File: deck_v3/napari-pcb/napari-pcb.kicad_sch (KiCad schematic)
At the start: 62 parts, among them J1 USB_C_Receptacle_USB2.0_16P, J11 DNP, J12 CONN_PB_SIG, J13 CONN_PB_GND, J14 CONN_PB_VDD, J17 CONN_PD_SIG, J18 CONN_GND, J19 CONN_VDD, J2 Cirque, J20 CONN_PD_GND, J21 CONN_PD_VDD, J3 Cirque, J4 CONN_ENC_DEV, J5 Cirque A MCU, J6 CONN_ENC_MCU, J7 Cirque B MCU, J8 CONN_PA_SIG, J9 CONN_PA_GND, SW1 SW_Push, SW10 SW_Push, SW11 SW_Push, SW12 SW_Push, SW13 SW_Push, SW14 SW_Push, SW15 SW_Push, SW16 SW_Push, SW2 SW_Push, SW3 SW_Push, SW4 SW_Push, SW5 SW_Push, SW6 SW_Push, SW7 SW_Push, SW8 SW_Push, SW9 SW_Push, U1 STM32G0B1RETx, U2 LD1117S33TR_SOT223

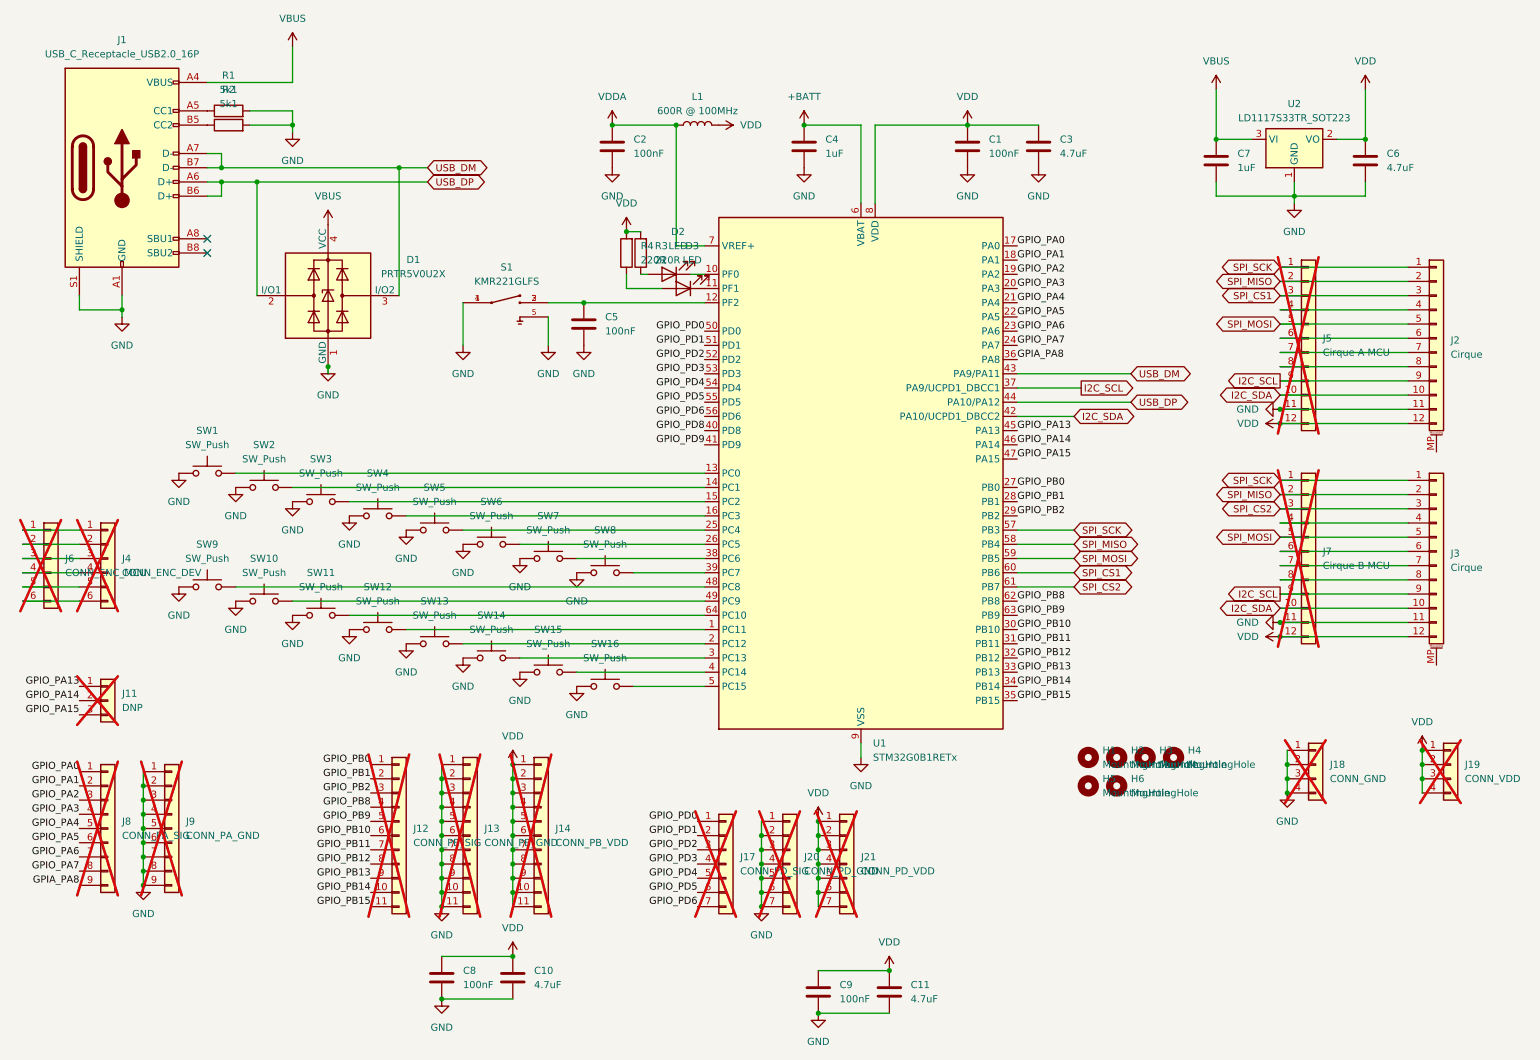
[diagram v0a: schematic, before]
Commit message: deck_v3: Tweak schematic layout for improved visibility of components.
No electrical change.

Signed-off-by: Damien George <dpgeorge@georgerobotics.com.au>
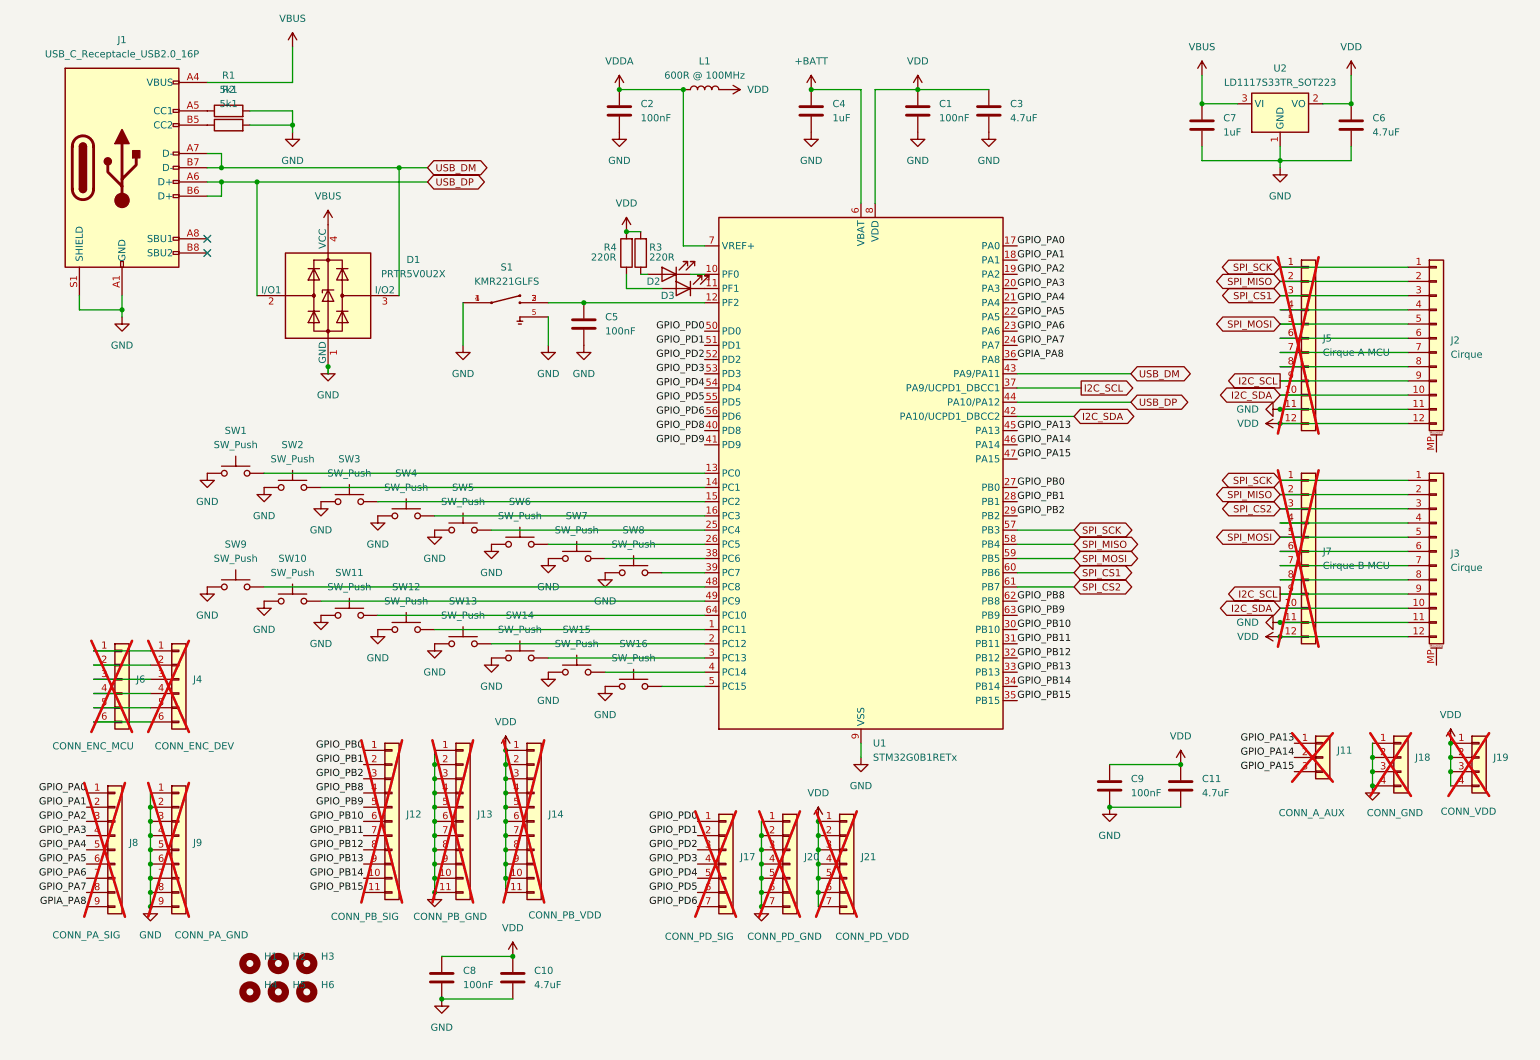
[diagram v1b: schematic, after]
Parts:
- J11: value DNP -> CONN_A_AUX
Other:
- company: (none) -> The napari project
- title: (none) -> Napari Deck
- moved on the sheet: C1, C11, C2, C3, C4, C6, C7, C9, H1, H2, H3, H4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
